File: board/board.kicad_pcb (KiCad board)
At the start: 2 copper layers, 21 x 29 mm, 10 parts, among them J1 002_SPI, J2 007_ADC, J3 007_ADC, U1 ADS131M03, X1 8MhZ

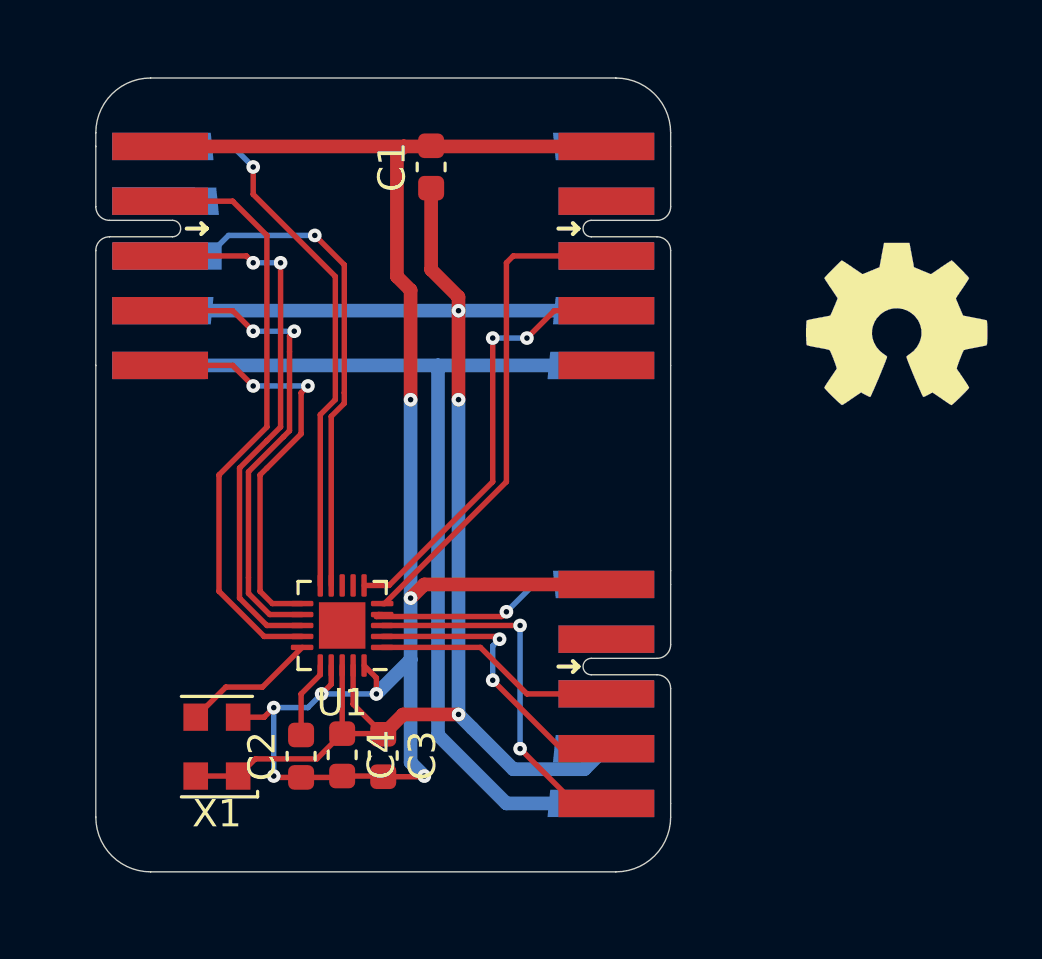
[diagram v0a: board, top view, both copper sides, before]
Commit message: fixed silkscreen
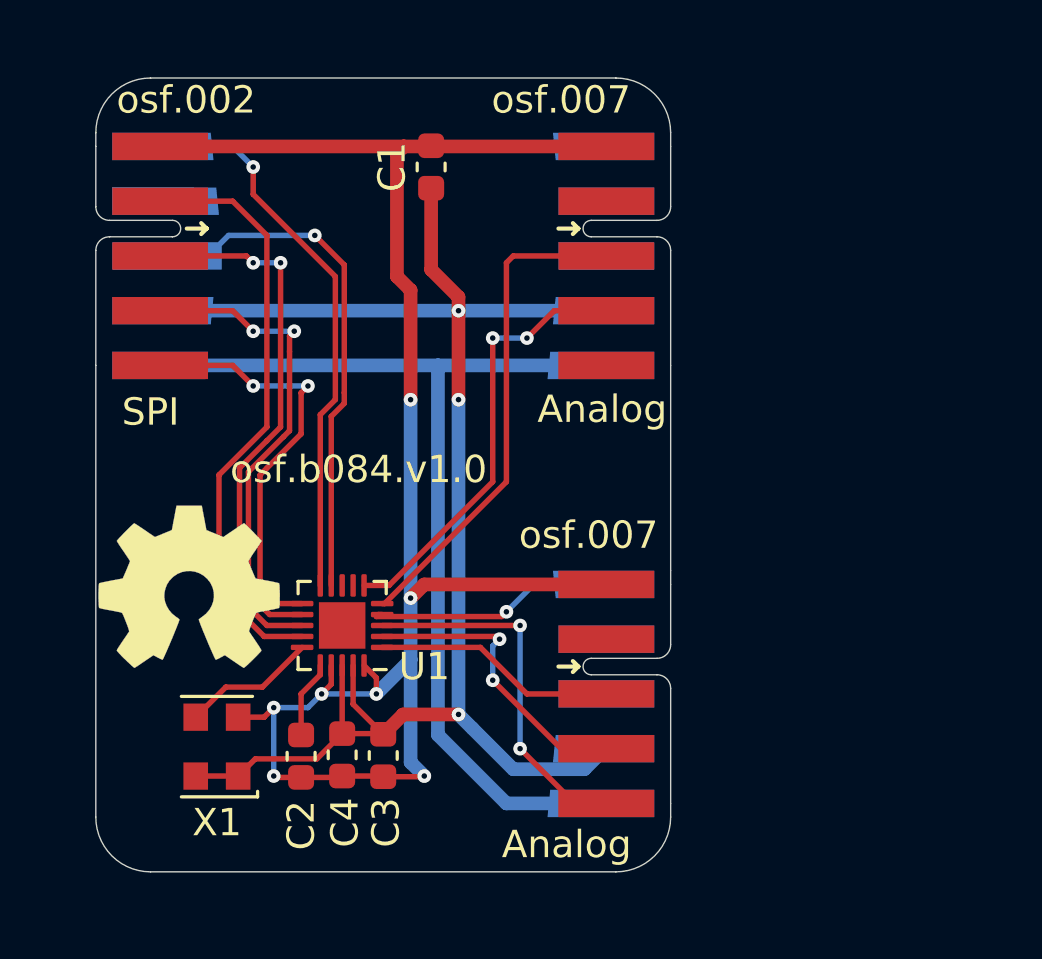
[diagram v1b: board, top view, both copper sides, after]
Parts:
- moved LOGO1 27.6 mm to (143.4, 108.6)
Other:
- board text added: "Analog"
- board text added: "SPI"
- board text added: "osf.002"
- board text added: "osf.007"
- board text added: "osf.b084.v1.0"
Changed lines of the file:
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@@
     (property "Sheetname" "adc")
     (attr smd)
-    (fp_text reference "C2" (at 0 -1.43 90) (layer "F.SilkS")
+    (fp_text reference "C2" (at -2.525 0 90) (layer "F.SilkS")
       (effects (font (size 1 1) (thickness 0.15)))
     )
@@
   )
   (footprint "Symbol:OSHW-Symbol_6.7x6mm_SilkScreen" (layer "F.Cu")
-    (at 169.25 99)
+    (at 143.4 108.6)
     (descr "Open Source Hardware Symbol")
     (tags "Logo Symbol OSHW")
@@
     (property "Sheetname" "adc")
     (attr smd)
-    (fp_text reference "X1" (at 0 -2.45) (layer "F.SilkS")
+    (fp_text reference "X1" (at 0 -2.775) (layer "F.SilkS")
       (effects (font (size 1 1) (thickness 0.15)))
     )
@@
     (property "Sheetname" "adc")
     (attr smd)
-    (fp_text reference "U1" (at 0 -2.82) (layer "F.SilkS")
+    (fp_text reference "U1" (at -3 -1.5) (layer "F.SilkS")
       (effects (font (size 1 1) (thickness 0.15)))
     )
@@
     (property "Sheetname" "adc")
     (attr smd)
-    (fp_text reference "C4" (at 0 -1.43 90) (layer "F.SilkS")
+    (fp_text reference "C4" (at 2.475 -0.1 90) (layer "F.SilkS")
       (effects (font (size 1 1) (thickness 0.15)))
     )
@@
     (property "Sheetname" "adc")
     (attr smd)
-    (fp_text reference "C3" (at 0 -1.43 90) (layer "F.SilkS")
+    (fp_text reference "C3" (at 2.45 -0.1 90) (layer "F.SilkS")
       (effects (font (size 1 1) (thickness 0.15)))
     )
@@
   (gr_line (start 161 108) (end 161 108.5) (layer "Edge.Cuts") (width 0.05))
   (gr_line (start 161 92.5) (end 161 92) (layer "Edge.Cuts") (width 0.05))
+  (gr_text "osf.b084.v1.0" (at 149.6 104.3) (layer "F.SilkS")
+    (effects (font (size 1 1) (thickness 0.15)))
+  )
+  (gr_text "Analog" (at 158.5 102.1) (layer "F.SilkS")
+    (effects (font (size 1 1) (thickness 0.15)))
+  )
+  (gr_text "SPI" (at 142 102.2) (layer "F.SilkS")
+    (effects (font (size 1 1) (thickness 0.15)))
+  )
+  (gr_text "Analog" (at 157.2 118) (layer "F.SilkS")
+    (effects (font (size 1 1) (thickness 0.15)))
+  )
+  (gr_text "osf.007" (at 158 106.7) (layer "F.SilkS")
+    (effects (font (size 1 1) (thickness 0.15)))
+  )
+  (gr_text "osf.002" (at 143.3 90.8) (layer "F.SilkS")
+    (effects (font (size 1 1) (thickness 0.15)))
+  )
+  (gr_text "osf.007" (at 157 90.8) (layer "F.SilkS")
+    (effects (font (size 1 1) (thickness 0.15)))
+  )
   (segment (start 153.25 98) (end 153.25 98.5) (width 0.5) (layer "F.Cu") (net 1))
   (segment (start 151.225 113.25) (end 150.5 113.975) (width 0.5) (layer "F.Cu") (net 1))

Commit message: added ground pours, a picture and decoupling for the oscillator
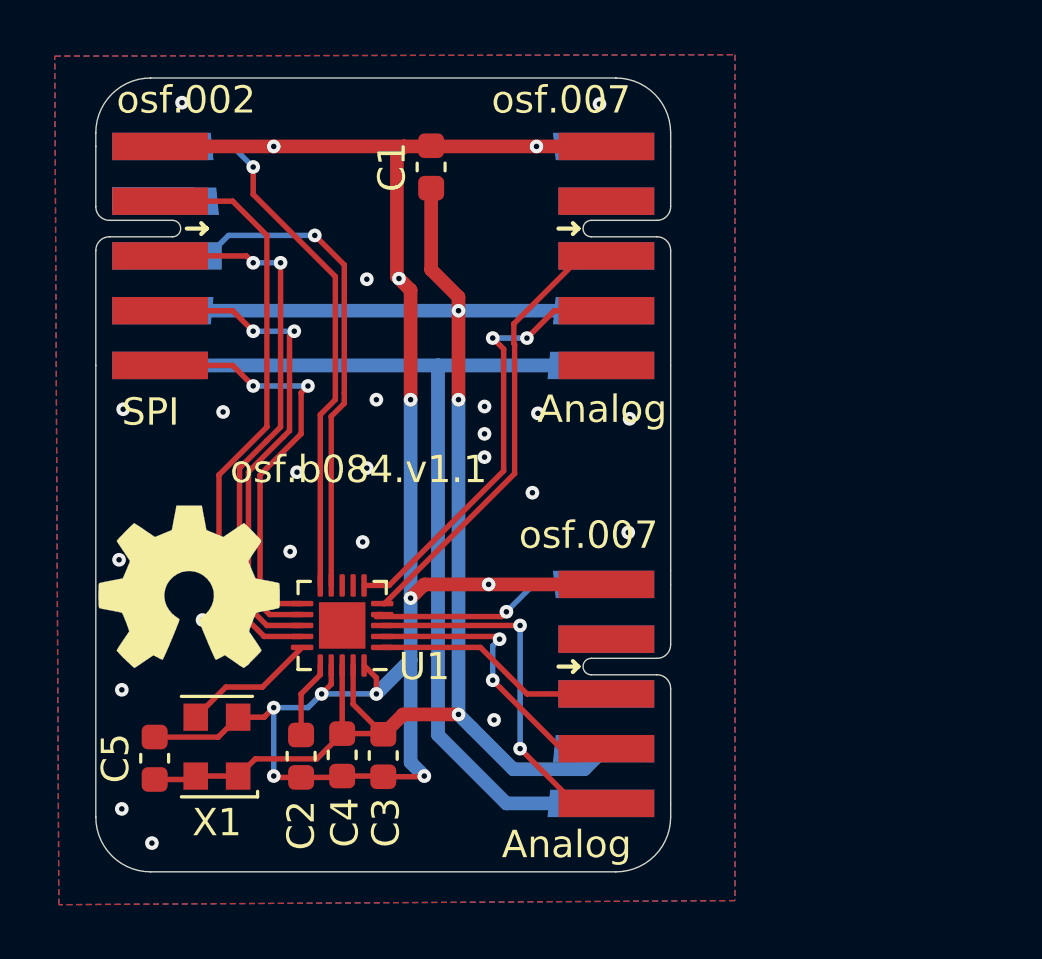
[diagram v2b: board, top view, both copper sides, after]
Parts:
- added C5: 100nF, Capacitor_SMD:C_0603_1608Metric, F.Cu at (142.2, 114.8)
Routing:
- net GND: track 64.8 -> 68.2 mm, vias 7 -> 35
- net /3.3V: track 58.3 -> 59.9 mm
- net /adc/AD3+: track 18.1 -> 16.7 mm
- added copper zone on B.Cu, net GND
- added copper zone on F.Cu, net GND
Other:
- board text added: "osf.b084.v1.1"
- board text removed: "osf.b084.v1.0"
